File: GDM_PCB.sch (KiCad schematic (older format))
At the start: 2 parts

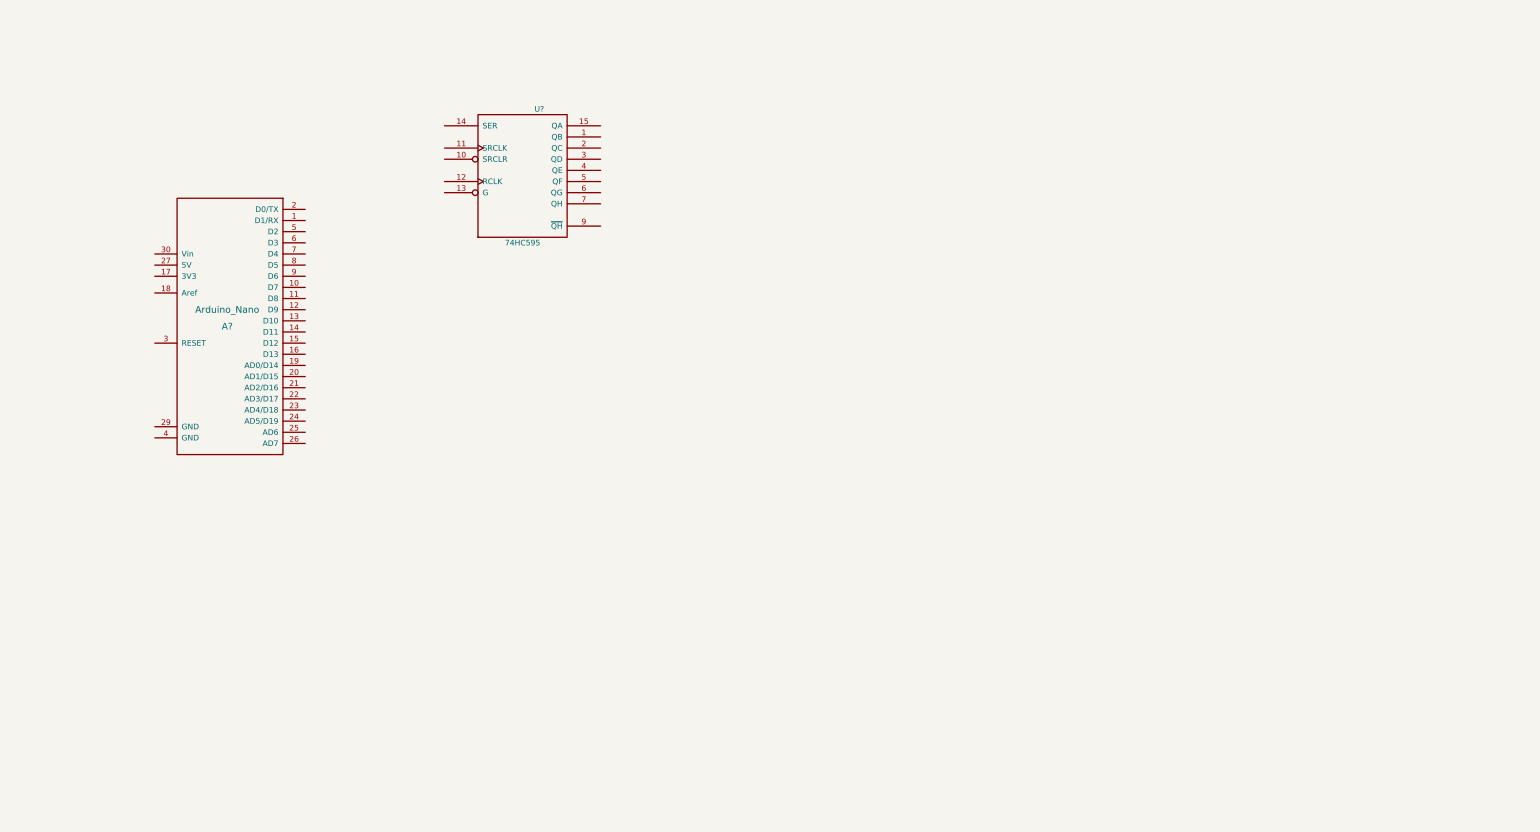
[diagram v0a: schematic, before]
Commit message: added stm32 and completed connection to 74hc595 and 7seg with resistors
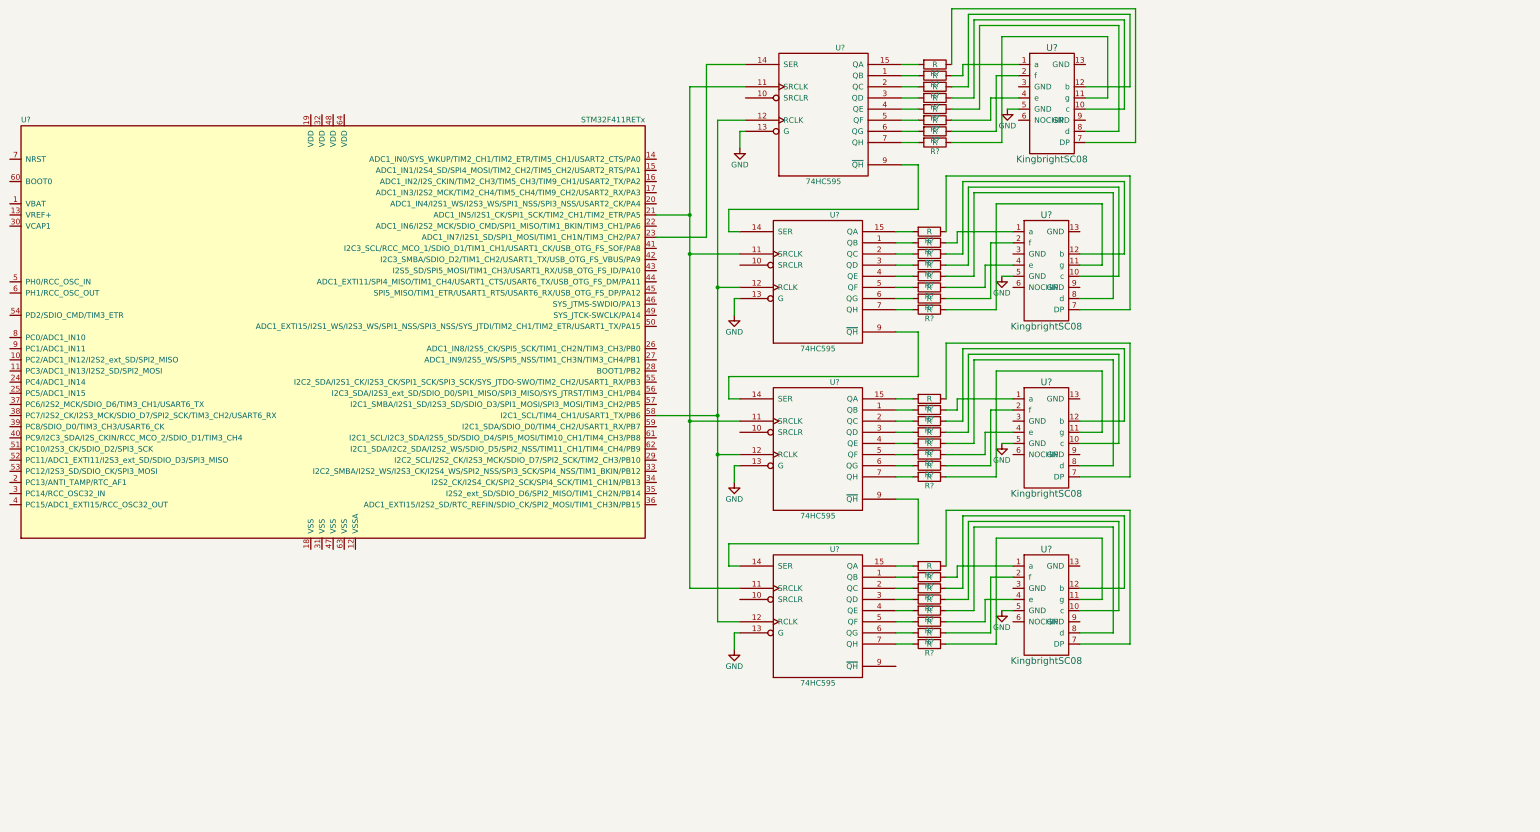
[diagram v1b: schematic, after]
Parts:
- removed A?: Arduino_Nano, symbol Arduino_Nano
- removed U?: 74HC595, symbol 74HC595
- added R? (x32): R, symbol R
- added U?: STM32F411RETx, LQFP64, symbol STM32F411RETx
- added U? (x4): 74HC595, symbol 74HC595
- added U? (x3): KingbrightSC08, symbol KingbrightSC08
- added U?: KingbrightSC08, Modules:kingbrightSC08, symbol KingbrightSC08
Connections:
- net GND: now also U?.13 (G), U?.13 (G), U?.13 (G), U?.13 (G), U?.5 (GND), U?.5 (GND), U?.5 (GND), U?.5 (GND), U?.8 (GND), U?.8 (GND), U?.8 (GND), U?.8 (GND)
- net VCC: now also U?.16 (VCC), U?.16 (VCC), U?.16 (VCC), U?.16 (VCC)
- new net: U?.11 (SRCLK), U?.11 (SRCLK), U?.11 (SRCLK), U?.11 (SRCLK), U?.21 (ADC1_IN5/I2S1_CK/SPI1_SCK/TIM2_CH1/TIM2_ETR/PA5)
- new net: U?.14 (SER), U?.23 (ADC1_IN7/I2S1_SD/SPI1_MOSI/TIM1_CH1N/TIM3_CH2/PA7)
- new net: U?.12 (RCLK), U?.12 (RCLK), U?.12 (RCLK), U?.12 (RCLK), U?.58 (I2C1_SCL/TIM4_CH1/USART1_TX/PB6)
- new net: R?.2, U?.1 (QB) (x4)
- new net: R?.2, U?.15 (QA) (x4)
- new net: R?.2, U?.2 (QC) (x4)
- new net: R?.2, U?.3 (QD) (x4)
- new net: R?.2, U?.4 (QE) (x4)
- new net: R?.2, U?.5 (QF) (x4)
- new net: R?.2, U?.6 (QG) (x4)
- new net: R?.2, U?.7 (QH) (x4)
- new net: U?.14 (SER), U?.9 (~QH) (x3)
- new net: R?.1, U?.7 (DP) (x4)
- new net: R?.1, U?.1 (a) (x4)
- new net: R?.1, U?.10 (c) (x4)
- new net: R?.1, U?.11 (g) (x4)
- new net: R?.1, U?.12 (b) (x4)
- new net: R?.1, U?.2 (f) (x4)
- new net: R?.1, U?.4 (e) (x4)
- new net: R?.1, U?.8 (d) (x4)

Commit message: completed nucleo f411re morpho connector footprint + library
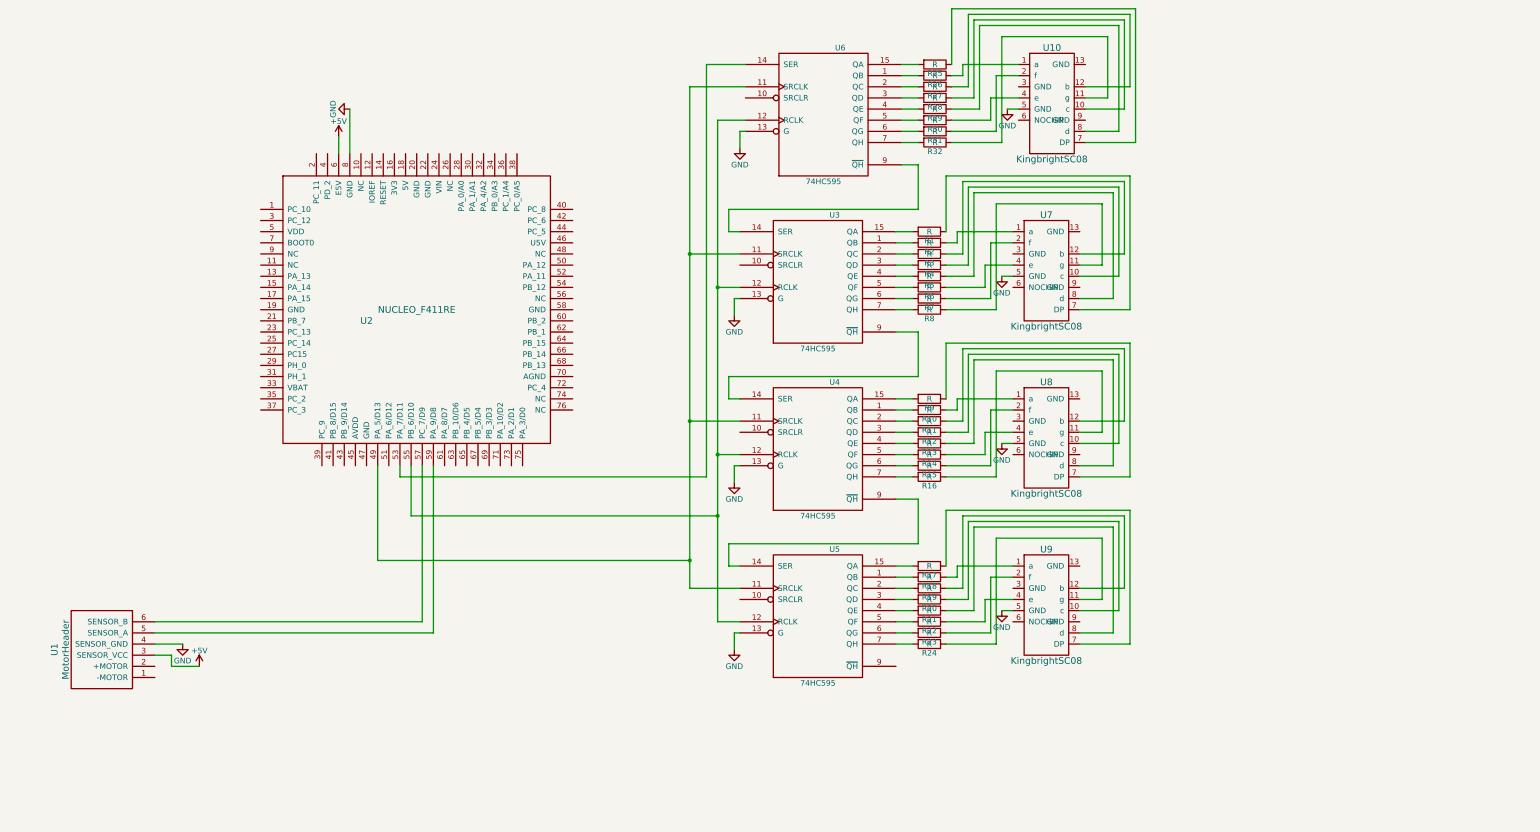
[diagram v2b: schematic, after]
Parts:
- removed U?: STM32F411RETx, LQFP64, symbol STM32F411RETx
- added U1: MotorHeader, symbol MotorHeader
- added U2: NUCLEO_F411RE, .pretty:NUCLEO_F411RE_MORPHO, symbol NUCLEO_F411RE
- U10, U8, U9: renamed from U?; footprint (none) -> .pretty:kingbrightSC08
- U3, U4, U5, U6: renamed from U?; footprint (none) -> .pretty:74HC595N
- U7: renamed from U?; footprint Modules:kingbrightSC08 -> .pretty:kingbrightSC08
- gave numbers to parts that had none: 32
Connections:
- net GND: now also U1.4 (SENSOR_GND), U2.8 (GND)
- net at U3.11 (SRCLK), U4.11 (SRCLK), U5.11 (SRCLK)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: now also U2.49 (PA_5/D13)
- net at U6.14 (SER): now also U2.53 (PA_7/D11)
- net at U3.12 (RCLK), U4.12 (RCLK), U5.12 (RCLK)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: now also U2.55 (PB_6/D10)
- new net: U1.6 (SENSOR_B), U2.57 (PC_7/D9)
- new net: U1.5 (SENSOR_A), U2.59 (PA_9/D8)
- new net +5V: U1.3 (SENSOR_VCC), U2.6 (E5V)

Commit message: finished footprints, connections, and PCB arrangement for 7seg setup
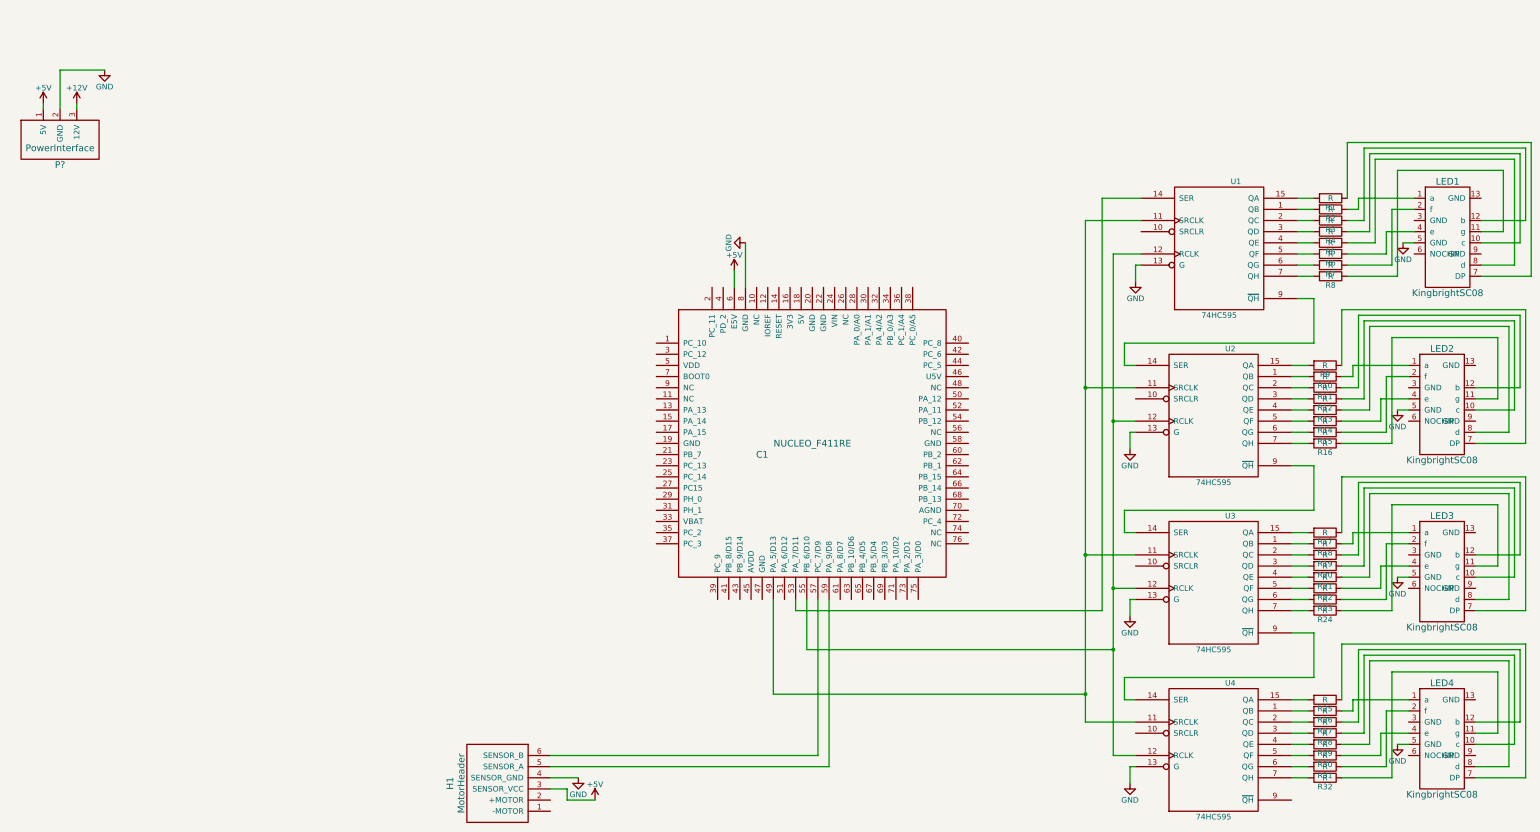
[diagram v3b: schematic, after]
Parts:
- added P?: PowerInterface, symbol PowerInterface
- R1, R10, R11, R12, R13, R14, R15, R16, R17, R18, R19, R2, R20, R21, R22, R23, R24, R25, R26, R27, R28, R29, R3, R30, R31, R32, R4, R5, R6, R7, R8, R9: footprint (none) -> .pretty:Resistor
- renumbered U2 to C1, U1 to H1, U10 to LED1, U7 to LED2, U8 to LED3, U9 to LED4, U6 to U1, U3 to U2, U4 to U3, U5 to U4
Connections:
- net +5V: now also P?.1 (5V)
- net GND: now also P?.2 (GND)
- net at U1.1 (QB): now also R2.2; no longer R26.2
- net at U1.15 (QA): now also R1.2; no longer R25.2
- net at U1.2 (QC): now also R3.2; no longer R27.2
- net at U1.3 (QD): now also R4.2; no longer R28.2
- net at U1.4 (QE): now also R5.2; no longer R29.2
- net at U1.5 (QF): now also R6.2; no longer R30.2
- net at U1.6 (QG): now also R7.2; no longer R31.2
- net at U1.7 (QH): now also R8.2; no longer R32.2
- net at R25.1: now also LED4.7 (DP); no longer LED1.7 (DP)
- net at LED1.1 (a): now also R2.1; no longer R26.1
- net at LED1.10 (c): now also R4.1; no longer R28.1
- net at LED1.11 (g): now also R8.1; no longer R32.1
- net at LED1.12 (b): now also R3.1; no longer R27.1
- net at LED1.2 (f): now also R7.1; no longer R31.1
- net at LED1.4 (e): now also R6.1; no longer R30.1
- net at LED1.8 (d): now also R5.1; no longer R29.1
- net at R1.1: now also LED1.7 (DP); no longer LED2.7 (DP)
- net at U2.15 (QA): now also R9.2; no longer R1.2
- net at LED2.1 (a): now also R10.1; no longer R2.1
- net at LED2.10 (c): now also R12.1; no longer R4.1
- net at LED2.11 (g): now also R16.1; no longer R8.1
- net at LED2.12 (b): now also R11.1; no longer R3.1
- net at LED2.2 (f): now also R15.1; no longer R7.1
- net at LED2.4 (e): now also R14.1; no longer R6.1
- net at LED2.8 (d): now also R13.1; no longer R5.1
- net at U2.1 (QB): now also R10.2; no longer R2.2
- net at U2.2 (QC): now also R11.2; no longer R3.2
- net at U2.3 (QD): now also R12.2; no longer R4.2
- net at U2.4 (QE): now also R13.2; no longer R5.2
- net at U2.5 (QF): now also R14.2; no longer R6.2
- net at U2.6 (QG): now also R15.2; no longer R7.2
- net at U2.7 (QH): now also R16.2; no longer R8.2
- net at R9.1: now also LED2.7 (DP); no longer LED3.7 (DP)
- net at U3.15 (QA): now also R17.2; no longer R9.2
- net at LED3.1 (a): now also R18.1; no longer R10.1
- net at LED3.10 (c): now also R20.1; no longer R12.1
- net at LED3.11 (g): now also R24.1; no longer R16.1
- net at LED3.12 (b): now also R19.1; no longer R11.1
- net at LED3.2 (f): now also R23.1; no longer R15.1
- net at LED3.4 (e): now also R22.1; no longer R14.1
- net at LED3.8 (d): now also R21.1; no longer R13.1
- net at U3.1 (QB): now also R18.2; no longer R10.2
- net at U3.2 (QC): now also R19.2; no longer R11.2
- net at U3.3 (QD): now also R20.2; no longer R12.2
- net at U3.4 (QE): now also R21.2; no longer R13.2
- net at U3.5 (QF): now also R22.2; no longer R14.2
- net at U3.6 (QG): now also R23.2; no longer R15.2
- net at U3.7 (QH): now also R24.2; no longer R16.2
- net at R17.1: now also LED3.7 (DP); no longer LED4.7 (DP)
- net at U4.15 (QA): now also R25.2; no longer R17.2
- net at LED4.1 (a): now also R26.1; no longer R18.1
- net at LED4.10 (c): now also R28.1; no longer R20.1
- net at LED4.11 (g): now also R32.1; no longer R24.1
- net at LED4.12 (b): now also R27.1; no longer R19.1
- net at LED4.2 (f): now also R31.1; no longer R23.1
- net at LED4.4 (e): now also R30.1; no longer R22.1
- net at LED4.8 (d): now also R29.1; no longer R21.1
- net at U4.1 (QB): now also R26.2; no longer R18.2
- net at U4.2 (QC): now also R27.2; no longer R19.2
- net at U4.3 (QD): now also R28.2; no longer R20.2
- net at U4.4 (QE): now also R29.2; no longer R21.2
- net at U4.5 (QF): now also R30.2; no longer R22.2
- net at U4.6 (QG): now also R31.2; no longer R23.2
- net at U4.7 (QH): now also R32.2; no longer R24.2
- new net +12V: P?.3 (12V)
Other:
- moved on the sheet: C1, H1, LED1, LED2, LED3, LED4, R1, R10, R11, R12, R13, R14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
